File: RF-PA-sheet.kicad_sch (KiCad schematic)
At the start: 42 parts, among them J7 SMA_F, J8 U.fl, U10 MHW720A, U14 PSA4-5043, U17 B39431B3710U410

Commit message: fixed broken schema symbols, removed buck12V output LEDs
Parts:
- C62: symbol Device:CP_Small -> Device:C_Polarized_Small
- NT1, NT2, NT3: symbol Device:Net-Tie_2 -> Device:NetTie_2
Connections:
- net GND: now also C62.2, NT2.2
- net at C46.2, C65.2, C99.2: now also NT1.1
- net at C100.2, C102.2, C45.1: now also NT3.2
- new net: NT1.2, NT2.1, NT3.1
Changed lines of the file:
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@@
     )
   )
-  (symbol (lib_id "Device:CP_Small") (at 137.16 76.2 0) (unit 1)
+  (symbol (lib_id "Device:C_Polarized_Small") (at 137.16 76.2 0) (unit 1)
     (in_bom yes) (on_board yes)
     (property "Reference" "C62" (id 0) (at 139.3952 75.0316 0)
@@
       (effects (font (size 1.27 1.27)) hide)
     )
+    (pin "1")
+    (pin "2")
   )
   (symbol (lib_id "power:GND") (at 143.51 44.45 0) (unit 1)
@@
     (pin "1")
   )
-  (symbol (lib_id "Device:Net-Tie_2") (at 69.85 121.92 0) (unit 1)
+  (symbol (lib_id "Device:NetTie_2") (at 69.85 121.92 0) (unit 1)
     (in_bom yes) (on_board yes)
     (property "Reference" "NT1" (id 0) (at 69.85 117.3226 0))
@@
       (effects (font (size 1.27 1.27)) hide)
     )
-  )
-  (symbol (lib_id "Device:Net-Tie_2") (at 80.01 121.92 0) (unit 1)
+    (pin "1")
+    (pin "2")
+  )
+  (symbol (lib_id "Device:NetTie_2") (at 80.01 121.92 0) (unit 1)
     (in_bom yes) (on_board yes)
     (property "Reference" "NT3" (id 0) (at 80.01 117.3226 0))
@@
       (effects (font (size 1.27 1.27)) hide)
     )
-  )
-  (symbol (lib_id "Device:Net-Tie_2") (at 74.93 128.27 270) (unit 1)
+    (pin "1")
+    (pin "2")
+  )
+  (symbol (lib_id "Device:NetTie_2") (at 74.93 128.27 270) (unit 1)
     (in_bom yes) (on_board yes)
     (property "Reference" "NT2" (id 0) (at 76.0476 127.1016 90)
@@
       (effects (font (size 1.27 1.27)) hide)
     )
+    (pin "1")
+    (pin "2")
   )
   (symbol (lib_id "Device:R_Small") (at 217.17 134.62 0) (mirror x) (unit 1)

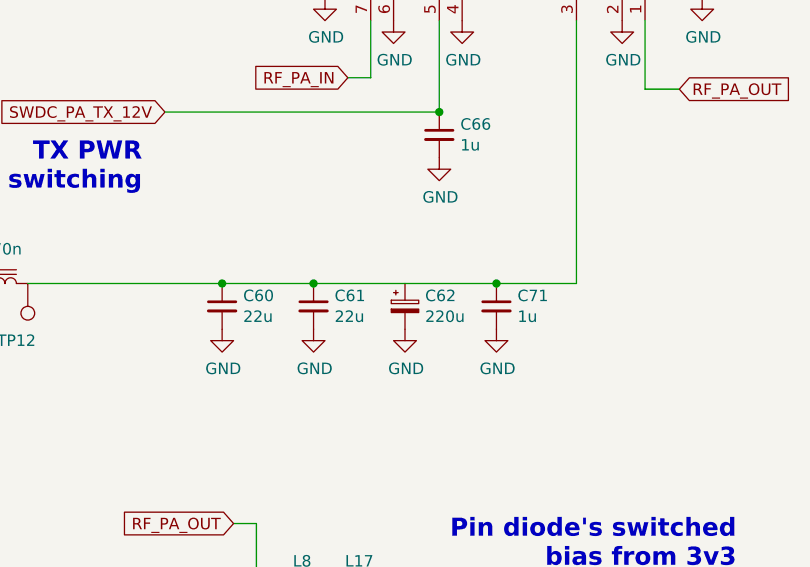
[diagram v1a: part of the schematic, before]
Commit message: RX and TX leds together, minor layout & silk fixes etc
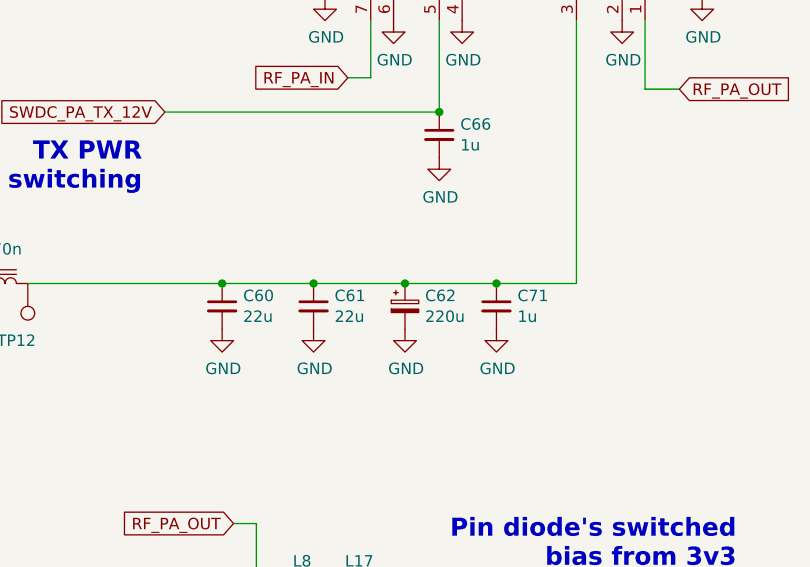
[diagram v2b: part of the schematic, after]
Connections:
- net at C62.1: now also C60.1, C61.1, C71.1, L6.2, TP12.1, U10.3 (Vs2)
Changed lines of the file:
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@@
   (junction (at 217.17 121.92) (diameter 0) (color 0 0 0 0)
+  )
+  (junction (at 137.16 73.66) (diameter 0) (color 0 0 0 0)
   )
   (junction (at 33.02 121.92) (diameter 0) (color 0 0 0 0)
@@
     (stroke (width 0) (type default) (color 0 0 0 0))
   )
-  (wire (pts (xy 127 73.66) (xy 147.32 73.66))
+  (wire (pts (xy 127 73.66) (xy 137.16 73.66))
     (stroke (width 0) (type default) (color 0 0 0 0))
   )
@@
     (stroke (width 0) (type default) (color 0 0 0 0))
   )
+  (wire (pts (xy 137.16 73.66) (xy 147.32 73.66))
+    (stroke (width 0) (type default) (color 0 0 0 0))
+  )

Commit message: misc
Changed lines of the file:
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@@
   )
   (global_label "SWDC_PA_TX_12V" (shape input) (at 110.49 54.61 180) (fields_autoplaced)
-    (effects (font (size 1.27 1.27)) (justify right))
-    (property "Intersheet References" "${INTERSHEET_REFS}" (id 0) (at 0 0 0)
-      (effects (font (size 1.27 1.27)) hide)
+    (effects (font (size 1.5 1.5) (thickness 0.3) bold) (justify right))
+    (property "Intersheet References" "${INTERSHEET_REFS}" (id 0) (at 88.4486 54.46 0)
+      (effects (font (size 1.5 1.5) (thickness 0.3) bold) (justify right) hide)
     )
   )
   (global_label "SWDC_PA_TX_3V3" (shape input) (at 154.94 109.22 0) (fields_autoplaced)
-    (effects (font (size 1.27 1.27)) (justify left))
-    (property "Intersheet References" "${INTERSHEET_REFS}" (id 0) (at 0 0 0)
-      (effects (font (size 1.27 1.27)) hide)
+    (effects (font (size 1.5 1.5) (thickness 0.3) bold) (justify left))
+    (property "Intersheet References" "${INTERSHEET_REFS}" (id 0) (at 176.9814 109.07 0)
+      (effects (font (size 1.5 1.5) (thickness 0.3) bold) (justify left) hide)
     )
   )
   (global_label "RF_PA_OUT" (shape input) (at 167.64 52.07 0) (fields_autoplaced)
-    (effects (font (size 1.27 1.27)) (justify left))
-    (property "Intersheet References" "${INTERSHEET_REFS}" (id 0) (at 0 0 0)
-      (effects (font (size 1.27 1.27)) hide)
+    (effects (font (size 1.5 1.5) (thickness 0.3) bold) (justify left))
+    (property "Intersheet References" "${INTERSHEET_REFS}" (id 0) (at 182.7529 51.92 0)
+      (effects (font (size 1.5 1.5) (thickness 0.3) bold) (justify left) hide)
     )
   )
   (global_label "12V_TO_RFPA" (shape input) (at 60.96 73.66 180) (fields_autoplaced)
-    (effects (font (size 1.27 1.27)) (justify right))
-    (property "Intersheet References" "${INTERSHEET_REFS}" (id 0) (at 0 0 0)
-      (effects (font (size 1.27 1.27)) hide)
+    (effects (font (size 1.5 1.5) (thickness 0.3) bold) (justify right))
+    (property "Intersheet References" "${INTERSHEET_REFS}" (id 0) (at 43.2757 73.51 0)
+      (effects (font (size 1.5 1.5) (thickness 0.3) bold) (justify right) hide)
     )
   )
   (global_label "RXP_FROM_LNA" (shape input) (at 275.59 125.73 270) (fields_autoplaced)
-    (effects (font (size 1.27 1.27)) (justify right))
-    (property "Intersheet References" "${INTERSHEET_REFS}" (id 0) (at 0 0 0)
-      (effects (font (size 1.27 1.27)) hide)
+    (effects (font (size 1.5 1.5) (thickness 0.3) bold) (justify right))
+    (property "Intersheet References" "${INTERSHEET_REFS}" (id 0) (at 275.44 145.5571 90)
+      (effects (font (size 1.5 1.5) (thickness 0.3) bold) (justify right) hide)
     )
   )
   (global_label "SWDC_LNA_3V3" (shape input) (at 217.17 95.25 0) (fields_autoplaced)
-    (effects (font (size 1.27 1.27)) (justify left))
-    (property "Intersheet References" "${INTERSHEET_REFS}" (id 0) (at 0 0 0)
-      (effects (font (size 1.27 1.27)) hide)
+    (effects (font (size 1.5 1.5) (thickness 0.3) bold) (justify left))
+    (property "Intersheet References" "${INTERSHEET_REFS}" (id 0) (at 236.7829 95.1 0)
+      (effects (font (size 1.5 1.5) (thickness 0.3) bold) (justify left) hide)
     )
   )
   (global_label "RF_PA_IN" (shape input) (at 130.81 50.8 180) (fields_autoplaced)
-    (effects (font (size 1.27 1.27)) (justify right))
-    (property "Intersheet References" "${INTERSHEET_REFS}" (id 0) (at 0 0 0)
-      (effects (font (size 1.27 1.27)) hide)
+    (effects (font (size 1.5 1.5) (thickness 0.3) bold) (justify right))
+    (property "Intersheet References" "${INTERSHEET_REFS}" (id 0) (at 117.6971 50.65 0)
+      (effects (font (size 1.5 1.5) (thickness 0.3) bold) (justify right) hide)
     )
   )
   (global_label "RF_PA_OUT" (shape input) (at 118.11 100.33 180) (fields_autoplaced)
-    (effects (font (size 1.27 1.27)) (justify right))
-    (property "Intersheet References" "${INTERSHEET_REFS}" (id 0) (at 0 0 0)
-      (effects (font (size 1.27 1.27)) hide)
+    (effects (font (size 1.5 1.5) (thickness 0.3) bold) (justify right))
+    (property "Intersheet References" "${INTERSHEET_REFS}" (id 0) (at 102.9971 100.18 0)
+      (effects (font (size 1.5 1.5) (thickness 0.3) bold) (justify right) hide)
     )
   )

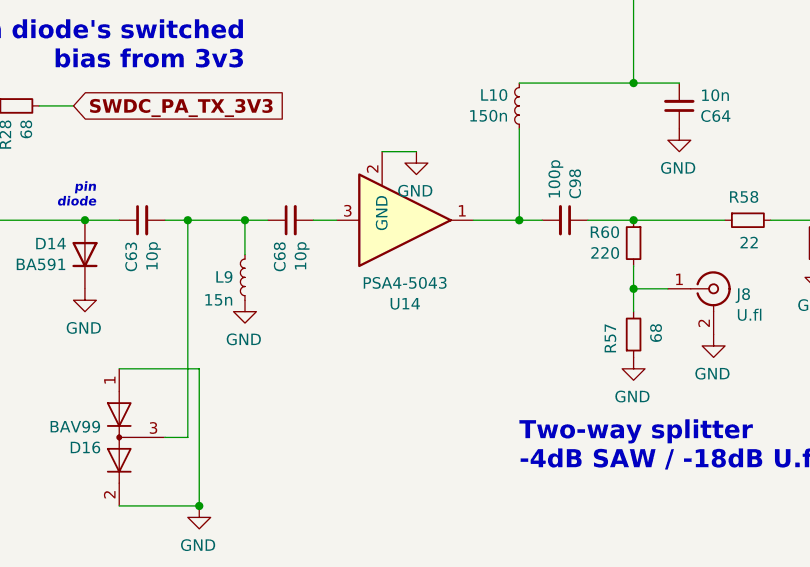
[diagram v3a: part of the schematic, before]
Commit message: PSA4-5043 -> SPF5043Z (removed silk text, added LCSC code, added paste back)
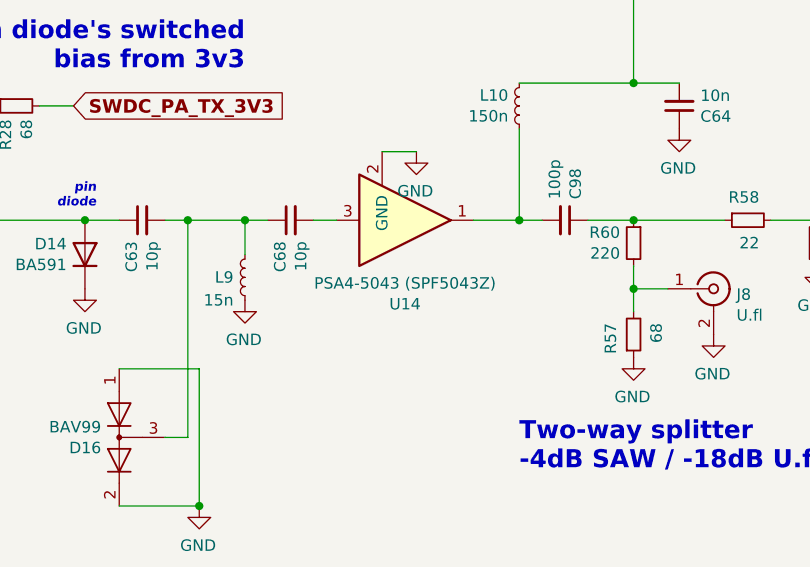
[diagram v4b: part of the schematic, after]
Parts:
- U14: value PSA4-5043 -> PSA4-5043 (SPF5043Z); DNP TRUE -> (none); LCSC (none) -> C470902
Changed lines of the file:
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@@
     (in_bom yes) (on_board yes)
     (property "Reference" "U14" (id 0) (at 191.77 131.2418 0))
-    (property "Value" "PSA4-5043" (id 1) (at 191.77 128.9304 0))
+    (property "Value" "PSA4-5043 (SPF5043Z)" (id 1) (at 191.77 128.9304 0))
     (property "Footprint" "Package_TO_SOT_SMD:SOT-343_SC-70-4_Handsoldering" (id 2) (at 191.77 121.92 0)
       (effects (font (size 1.27 1.27)) hide)
     )
-    (property "Datasheet" "" (id 3) (at 191.77 121.92 0)
+    (property "Datasheet" "https://datasheet.lcsc.com/lcsc/1912181407_Qorvo-SPF5043Z_C470902.pdf" (id 3) (at 191.77 121.92 0)
       (effects (font (size 1.27 1.27)) hide)
     )
-    (property "DNP" "TRUE" (id 4) (at 191.77 121.92 0)
+    (property "LCSC" "C470902" (id 4) (at 191.77 121.92 0)
       (effects (font (size 1.27 1.27)) hide)
     )

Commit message: return paste back to SAW as will be assembled
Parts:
- U17: DNP TRUE -> (none)
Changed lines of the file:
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@@
       (effects (font (size 1.27 1.27)) hide)
     )
-    (property "DNP" "TRUE" (id 4) (at 260.35 121.92 0)
+    (property "DNP" "" (id 4) (at 260.35 121.92 0)
       (effects (font (size 1.27 1.27)) hide)
     )

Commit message: LCSC codes changed (out-of-stock parts)
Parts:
- C100, C102, C47, C65, C69, C99: LCSC C519956 -> C519994
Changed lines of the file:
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@@
       (effects (font (size 1.27 1.27)) hide)
     )
-    (property "LCSC" "C519956" (id 4) (at 140.97 124.46 0)
+    (property "LCSC" "C519994" (id 4) (at 140.97 124.46 0)
       (effects (font (size 1.27 1.27)) hide)
     )
@@
       (effects (font (size 1.27 1.27)) hide)
     )
-    (property "LCSC" "C519956" (id 4) (at 57.15 124.46 0)
+    (property "LCSC" "C519994" (id 4) (at 57.15 124.46 0)
       (effects (font (size 1.27 1.27)) hide)
     )
@@
       (effects (font (size 1.27 1.27)) hide)
     )
-    (property "LCSC" "C519956" (id 4) (at 120.65 129.54 0)
+    (property "LCSC" "C519994" (id 4) (at 120.65 129.54 0)
       (effects (font (size 1.27 1.27)) hide)
     )
@@
       (effects (font (size 1.27 1.27)) hide)
     )
-    (property "LCSC" "C519956" (id 4) (at 92.71 124.46 0)
+    (property "LCSC" "C519994" (id 4) (at 92.71 124.46 0)
       (effects (font (size 1.27 1.27)) hide)
     )
@@
       (effects (font (size 1.27 1.27)) hide)
     )
-    (property "LCSC" "C519956" (id 4) (at 102.87 124.46 0)
+    (property "LCSC" "C519994" (id 4) (at 102.87 124.46 0)
       (effects (font (size 1.27 1.27)) hide)
     )
@@
       (effects (font (size 1.27 1.27)) hide)
     )
-    (property "LCSC" "C519956" (id 4) (at 49.53 124.46 0)
-      (effects (font (size 1.27 1.27)) hide)
-    )
+    (property "LCSC" "C519994" (id 4) (at 49.53 124.46 0)
+      (effects (font (size 1.27 1.27)) hide)
+    )
